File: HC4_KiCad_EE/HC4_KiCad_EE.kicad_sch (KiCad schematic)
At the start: 11 parts, among them J1 USB_B_Mini

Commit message: たぶん完成！！！！！！！
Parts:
- LD2: value Carry -> LED
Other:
- title: HC4_CPU -> HC4e_CPU
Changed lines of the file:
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@@
 	(paper "A4")
 	(title_block
-		(title "HC4_CPU")
-		(date "2025-06-16")
+		(title "HC4e_CPU")
+		(date "2025-07-21")
 		(rev "1.0")
 	)
@@
 			)
 		)
-		(property "Value" "Carry"
+		(property "Value" "LED"
 			(at 273.05 90.4874 90)
 			(effects

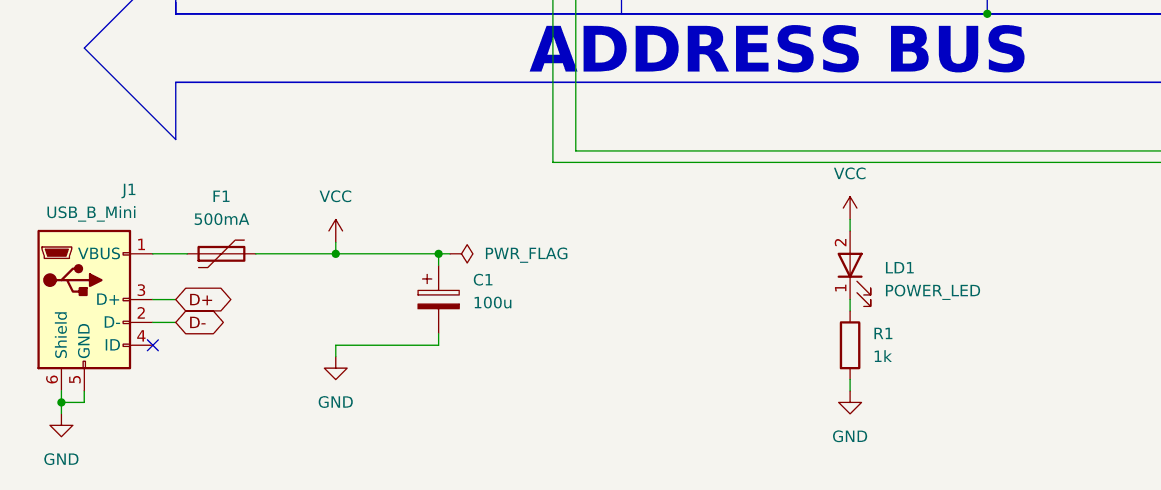
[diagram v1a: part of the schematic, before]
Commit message: HC4e設計変更:CH340に敗北宣言、USBシリアル仕様に変更
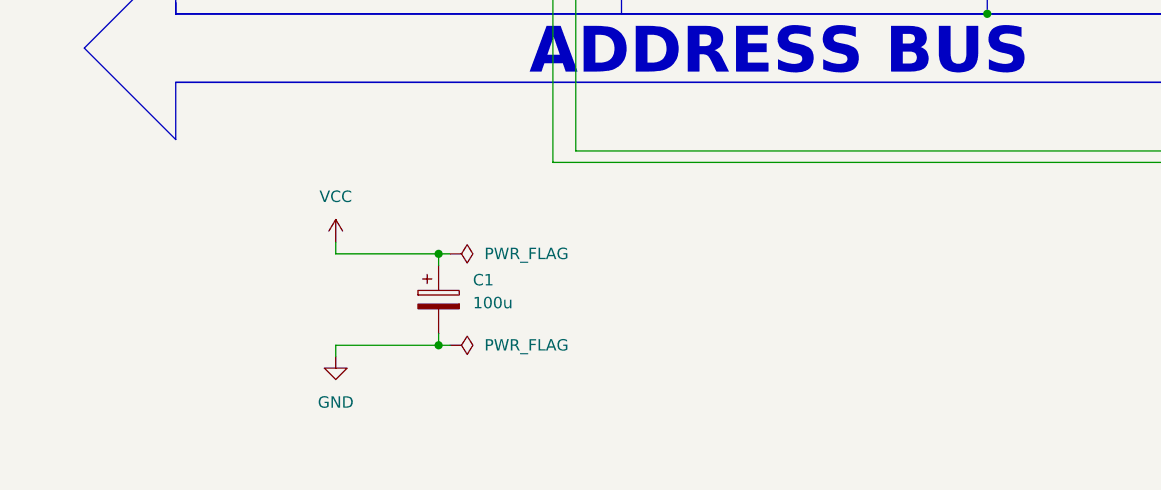
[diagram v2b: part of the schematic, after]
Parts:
- removed F1: 500mA, Fuse:Fuse_Bourns_MF-RG400, symbol Device:Polyfuse
- removed J1: USB_B_Mini, Connector_USB:USB_Mini-B_Wuerth_65100516121_Horizontal, symbol Connector:USB_B_Mini
- removed LD1: POWER_LED, LED_THT:LED_D5.0mm, symbol Device2:LED_
- removed R1: 1k, Resistor_SMD:R_0603_1608Metric, symbol Device:R
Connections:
- no-connect marks 1 -> 0

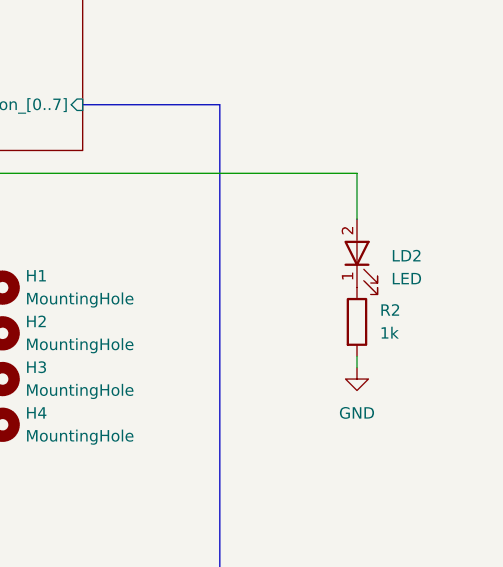
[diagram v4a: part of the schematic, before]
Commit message: feat:HC4e改版,BOMを令和最新版に更新,KiCadを10に更新
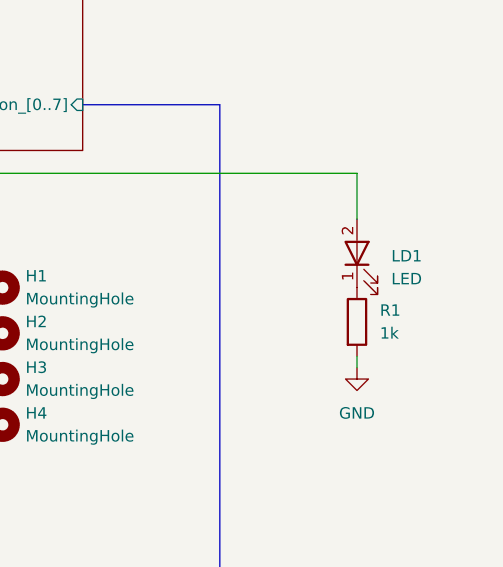
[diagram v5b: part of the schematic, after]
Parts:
- renumbered LD2 to LD1, R2 to R1

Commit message: 基板を若干改版、フットプリントの指定が外れていたのを修正
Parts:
- R1: LCSC PN (none) -> C21190
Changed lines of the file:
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@@
+			)
+		)
+		(property "LCSC PN" "C21190"
+			(at 269.24 95.25 0)
+			(hide yes)
+			(show_name no)
+			(do_not_autoplace no)
+			(effects
+				(font
+					(size 1.27 1.27)
+				)
 			)
 		)
@@
 			)
 		)
+		(property "LCSC PN" ""
+			(at 229.87 96.52 0)
+			(hide yes)
+			(show_name no)
+			(do_not_autoplace no)
+			(effects
+				(font
+					(size 1.27 1.27)
+				)
+			)
+		)
 		(instances
 			(project "HC4_KiCad_EE"
@@
 			)
 		)
+		(property "LCSC PN" ""
+			(at 229.87 91.44 0)
+			(hide yes)
+			(show_name no)
+			(do_not_autoplace no)
+			(effects
+				(font
+					(size 1.27 1.27)
+				)
+			)
+		)
 		(instances
 			(project "HC4_KiCad_EE"
@@
 			)
 		)
+		(property "LCSC PN" ""
+			(at 59.69 176.53 0)
+			(hide yes)
+			(show_name no)
+			(do_not_autoplace no)
+			(effects
+				(font
+					(size 1.27 1.27)
+				)
+			)
+		)
 		(pin "2"
 		)
@@
 			)
 		)
+		(property "LCSC PN" ""
+			(at 229.87 106.68 0)
+			(hide yes)
+			(show_name no)
+			(do_not_autoplace no)
+			(effects
+				(font
+					(size 1.27 1.27)
+				)
+			)
+		)
 		(instances
 			(project "HC4_KiCad_EE"
@@
 			)
 		)
+		(property "LCSC PN" ""
+			(at 269.24 87.63 90)
+			(hide yes)
+			(show_name no)
+			(do_not_autoplace no)
+			(effects
+				(font
+					(size 1.27 1.27)
+				)
+			)
+		)
 		(pin "2"
 		)
@@
 			(at 229.87 101.6 0)
 			(hide yes)
+			(show_name no)
+			(do_not_autoplace no)
+			(effects
+				(font
+					(size 1.27 1.27)
+				)
+			)
+		)
+		(property "LCSC PN" ""
+			(at 229.87 101.6 0)
+			(hide yes)

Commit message: HC4eRev2完成
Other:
- company: (none) -> Dengiken
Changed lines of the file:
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@@
 	(title_block
 		(title "HC4e_CPU")
-		(date "2026-03-19")
+		(date "2026-05-23")
 		(rev "2.0")
+		(company "Dengiken")
 	)
 	(rectangle
